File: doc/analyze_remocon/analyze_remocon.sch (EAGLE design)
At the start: 15 parts, among them IC3 PIC18F2550_28DIP, T1 2SC1815, X1 MINI-USB-UX60-MB-5S8

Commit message: update circuit diagram documents
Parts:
- removed C3, C4: (no value), rcl:C-EU025-024X044
- removed D1, D2: SFH482, led:SFH482
- removed JP1: (no value), pinhead:PINHD-1X5/90
- removed Q1: (no value), special:XTAL/S
- removed S1: PVA1R, switch-misc:PVA1R
- removed T1: 2SC1815, transistor:2SC1815
- added IRLED, IRLED1: (no value), led:LED3MM
- added Q2: BUZ11BV, transistor-power:BUZ11BV
- added R1, R2, R6, R7: (no value), rcl:R-US_MELF0102R
- added R10, R8, R9: (no value), rcl:R-US_0207/7
- added SW1, SW2: (no value), switch-omron:10-XX
- added Y1: (no value), xtal:CRES-HA
- C1, C2: device rcl:C-EU025-024X044 -> rcl:C-EUC0603K
- LED1, LED2: value LAP4-BOTTOM -> (none); device led:LAP4-BOTTOM -> led:LED3MM
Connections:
- removed net +5V: X1.1
- new net 20MHZ: IC3.OSC1/CLKI, Y1.LFT
- new net BLOCK: C1.1, IC3.VDD, R1.2, R10.2, R2.2, U$1.VCC, X1.1
- new net N$10: C2.1, IC3.VUSB
- new net N$11: LED1.A, R6.1
- new net N$12: IC3.RA5/AN4/!SS!/HLVDIN/C2OUT, R7.2
- new net N$13: LED2.A, R7.1
- new net N$14: IC3.RA0/AN0, R8.2, R9.1
- new net N$15: IRLED.A, R10.1
- new net N$16: IRLED.C, IRLED1.A
- new net N$17: IRLED1.C, Q2.D
- new net N$18: Q2.G, R9.2
- new net N$3: R1.1, SW1.P
- new net N$4: IC3.!MCLR!/VPP/RE3, SW1.P1
- new net N$5: R2.1, SW2.P
- new net N$6: IC3.RB4/AN11/KBI0/CSSPP, SW2.P1
- new net N$7: IC3.RB3/AN9/CCP2/VPO, U$1.VOUT
- new net N$8: IC3.RA6/OSC2/CLKO, Y1.RIT
- new net N$9: IC3.RA4/T0CKI/CIOUT/RCV, R6.2
- net GND: now also C1.2, C2.2, IC3.VSS, IC3.VSS@1, LED1.C, LED2.C, Q2.S, R8.1, SW1.S1, SW2.S1, U$1.GND, Y1.GND
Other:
- moved on the sheet: C1, C2, IC3, LED1, LED2, X1

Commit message: update circuit diagram documents
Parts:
- removed C1: (no value), rcl:C-EUC0603K
- added C3: (no value), rcl:C-EU025-025X050
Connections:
- removed net N$3: R1.1, SW1.P
- removed net N$5: R2.1, SW2.P
- removed net N$6: IC3.RB4/AN11/KBI0/CSSPP, SW2.P1
- new net N$7: IC3.RB4/AN11/KBI0/CSSPP, R2.1, SW2.P
- net BLOCK: now also C3.1; no longer C1.1
- net GND: now also C3.2, SW2.S; no longer C1.2
- net N$4: now also R1.1
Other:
- moved on the sheet: SW1, SW2
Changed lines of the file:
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@@
 <part name="LED2" library="led" deviceset="LED" device="3MM"/>
 <part name="Y1" library="xtal" deviceset="CRES-H" device="A"/>
-<part name="C1" library="rcl" deviceset="C-EU" device="C0603K"/>
 <part name="C2" library="rcl" deviceset="C-EU" device="C0603K"/>
 <part name="R1" library="rcl" deviceset="R-US_" device="MELF0102R"/>
@@
 <part name="R10" library="rcl" deviceset="R-US_" device="0207/7"/>
 <part name="Q2" library="transistor-power" deviceset="BUZ11" device="BV"/>
+<part name="C3" library="rcl" deviceset="C-EU" device="025-025X050"/>
+<part name="SUPPLY17" library="supply2" deviceset="GND" device=""/>
 </parts>
 <sheets>
@@
 <instance part="SUPPLY3" gate="+5V" x="96.52" y="17.78"/>
 <instance part="SUPPLY4" gate="GND" x="96.52" y="2.54"/>
-<instance part="SW1" gate="1" x="10.16" y="53.34" rot="R270"/>
-<instance part="SW2" gate="1" x="81.28" y="43.18" rot="R270"/>
+<instance part="SW1" gate="1" x="7.62" y="53.34" rot="R270"/>
+<instance part="SW2" gate="1" x="83.82" y="43.18" rot="R270"/>
 <instance part="SUPPLY5" gate="+5V" x="0" y="66.04"/>
-<instance part="SUPPLY6" gate="GND" x="15.24" y="48.26"/>
+<instance part="SUPPLY6" gate="GND" x="12.7" y="48.26"/>
 <instance part="SUPPLY7" gate="+5V" x="71.12" y="55.88"/>
 <instance part="SUPPLY8" gate="+5V" x="116.84" y="30.48"/>
 <instance part="SUPPLY9" gate="GND" x="104.14" y="27.94"/>
-<instance part="SUPPLY10" gate="GND" x="86.36" y="38.1"/>
+<instance part="SUPPLY10" gate="GND" x="88.9" y="38.1"/>
 <instance part="SUPPLY11" gate="GND" x="-12.7" y="-5.08"/>
 <instance part="SUPPLY12" gate="GND" x="-53.34" y="2.54"/>
@@
 <instance part="LED2" gate="G$1" x="-45.72" y="12.7" rot="R270"/>
 <instance part="Y1" gate="G$1" x="-30.48" y="-2.54"/>
-<instance part="C1" gate="G$1" x="96.52" y="12.7"/>
 <instance part="C2" gate="G$1" x="-5.08" y="2.54" rot="R270"/>
 <instance part="R1" gate="G$1" x="0" y="58.42" rot="R90"/>
@@
 <instance part="R10" gate="G$1" x="-15.24" y="71.12" rot="R90"/>
 <instance part="Q2" gate="1" x="-17.78" y="45.72"/>
+<instance part="C3" gate="G$1" x="96.52" y="12.7"/>
+<instance part="SUPPLY17" gate="GND" x="91.44" y="40.64"/>
 </instances>
 <busses>
@@
 <pinref part="SUPPLY3" gate="+5V" pin="+5V"/>
 <wire x1="73.66" y1="15.24" x2="96.52" y2="15.24" width="0.1524" layer="91"/>
-<pinref part="C1" gate="G$1" pin="1"/>
+<pinref part="C3" gate="G$1" pin="1"/>
 <junction x="96.52" y="15.24"/>
 </segment>
@@
 <pinref part="SUPPLY4" gate="GND" pin="GND"/>
 <wire x1="96.52" y1="7.62" x2="96.52" y2="5.08" width="0.1524" layer="91"/>
-<pinref part="C1" gate="G$1" pin="2"/>
+<pinref part="C3" gate="G$1" pin="2"/>
 <junction x="96.52" y="7.62"/>
 </segment>
@@
 <pinref part="SUPPLY15" gate="GND" pin="GND"/>
 </segment>
+<segment>
+<pinref part="SW2" gate="1" pin="S"/>
+<pinref part="SUPPLY17" gate="GND" pin="GND"/>
+<wire x1="88.9" y1="43.18" x2="91.44" y2="43.18" width="0.1524" layer="91"/>
+</segment>
 </net>
 <net name="N$1" class="0">
@@
 </segment>
 </net>
-<net name="N$5" class="0">
-<segment>
-<pinref part="SW2" gate="1" pin="P"/>
-<wire x1="71.12" y1="43.18" x2="76.2" y2="43.18" width="0.1524" layer="91"/>
-<pinref part="R2" gate="G$1" pin="1"/>
-</segment>
-</net>
-<net name="N$6" class="0">
-<segment>
-<pinref part="IC3" gate="G$1" pin="RB4/AN11/KBI0/CSSPP"/>
-<pinref part="SW2" gate="1" pin="P1"/>
-<wire x1="73.66" y1="27.94" x2="76.2" y2="27.94" width="0.1524" layer="91"/>
-<wire x1="76.2" y1="27.94" x2="76.2" y2="40.64" width="0.1524" layer="91"/>
-</segment>
-</net>
-<net name="N$7" class="0">
+<net name="N$19" class="0">
 <segment>
 <pinref part="IC3" gate="G$1" pin="RB3/AN9/CCP2/VPO"/>
@@
 <pinref part="SW1" gate="1" pin="P1"/>
 <pinref part="IC3" gate="G$1" pin="!MCLR!/VPP/RE3"/>
-<wire x1="5.08" y1="50.8" x2="-2.54" y2="50.8" width="0.1524" layer="91"/>
+<wire x1="2.54" y1="50.8" x2="0" y2="50.8" width="0.1524" layer="91"/>
+<wire x1="0" y1="50.8" x2="-2.54" y2="50.8" width="0.1524" layer="91"/>
 <wire x1="-2.54" y1="50.8" x2="-2.54" y2="35.56" width="0.1524" layer="91"/>
-</segment>
-</net>
-<net name="N$3" class="0">
-<segment>
-<pinref part="SW1" gate="1" pin="P"/>
-<wire x1="0" y1="53.34" x2="5.08" y2="53.34" width="0.1524" layer="91"/>
 <pinref part="R1" gate="G$1" pin="1"/>
+<wire x1="0" y1="50.8" x2="0" y2="53.34" width="0.1524" layer="91"/>
+<junction x="0" y="50.8"/>
 </segment>
 </net>
@@
 </segment>
 </net>
+<net name="N$7" class="0">
+<segment>
+<pinref part="SW2" gate="1" pin="P"/>
+<wire x1="71.12" y1="43.18" x2="76.2" y2="43.18" width="0.1524" layer="91"/>
+<pinref part="R2" gate="G$1" pin="1"/>
+<pinref part="IC3" gate="G$1" pin="RB4/AN11/KBI0/CSSPP"/>
+<wire x1="76.2" y1="43.18" x2="78.74" y2="43.18" width="0.1524" layer="91"/>
+<wire x1="73.66" y1="27.94" x2="76.2" y2="27.94" width="0.1524" layer="91"/>
+<wire x1="76.2" y1="27.94" x2="76.2" y2="43.18" width="0.1524" layer="91"/>
+<junction x="76.2" y="43.18"/>
+</segment>
+</net>

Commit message: update circuit diagram documents
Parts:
- removed C3: (no value), rcl:C-EU025-025X050
- removed R8, R9: (no value), rcl:R-US_0207/7
- added C1: 0.1uF, rcl:C-EU025-024X044
- added R3, R4: 1KΩ, rcl:R-US_MELF0102R
- C2: value (none) -> 0.1uF; device rcl:C-EUC0603K -> rcl:C-EU025-024X044
- IRLED1, IRLED2: value (none) -> TLN105B
- R1, R2: value (none) -> 10KΩ
- R5: value (none) -> 1Ω
- R6, R7: value (none) -> 10KΩ; device rcl:R-US_MELF0102R -> rcl:R-US_0207/7
- RESONATOR: value (none) -> 20MHz
- renumbered IRLED to IRLED2, Q2 to 2SK2201, R10 to R5, U$1 to PL-IRM2161-C438, Y1 to RESONATOR
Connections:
- net BLOCK: now also C1.1; no longer C3.1
- net GND: now also C1.2, R6.1; no longer C3.2, R8.1
- net N$11: now also R3.1; no longer R6.1
- net N$12: now also R4.2; no longer R7.2
- net N$13: now also R4.1; no longer R7.1
- net N$14: now also R6.2, R7.1; no longer R8.2, R9.1
- net N$18: now also R7.2; no longer R9.2
- net N$9: now also R3.2; no longer R6.2
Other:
- moved on the sheet: R6, R7
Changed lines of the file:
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@@
 <part name="IC3" library="microchip" deviceset="PIC18F2*_28" device="DIP" technology="550"/>
 <part name="X1" library="con-hirose" deviceset="MINI-USB-" device="UX60-MB-5S8"/>
-<part name="U$1" library="IRM2161" deviceset="IRM2161" device=""/>
+<part name="PL-IRM2161-C438" library="IRM2161" deviceset="IRM2161" device=""/>
 <part name="SUPPLY1" library="supply2" deviceset="GND" device=""/>
 <part name="SUPPLY2" library="supply2" deviceset="+5V" device=""/>
@@
 <part name="LED1" library="led" deviceset="LED" device="3MM"/>
 <part name="LED2" library="led" deviceset="LED" device="3MM"/>
-<part name="Y1" library="xtal" deviceset="CRES-H" device="A"/>
-<part name="C2" library="rcl" deviceset="C-EU" device="C0603K"/>
-<part name="R1" library="rcl" deviceset="R-US_" device="MELF0102R"/>
-<part name="R2" library="rcl" deviceset="R-US_" device="MELF0102R"/>
-<part name="R6" library="rcl" deviceset="R-US_" device="MELF0102R"/>
-<part name="R7" library="rcl" deviceset="R-US_" device="MELF0102R"/>
-<part name="IRLED" library="led" deviceset="LED" device="3MM"/>
-<part name="IRLED1" library="led" deviceset="LED" device="3MM"/>
-<part name="R8" library="rcl" deviceset="R-US_" device="0207/7"/>
-<part name="R9" library="rcl" deviceset="R-US_" device="0207/7"/>
-<part name="R10" library="rcl" deviceset="R-US_" device="0207/7"/>
-<part name="Q2" library="transistor-power" deviceset="BUZ11" device="BV"/>
-<part name="C3" library="rcl" deviceset="C-EU" device="025-025X050"/>
+<part name="RESONATOR" library="xtal" deviceset="CRES-H" device="A" value="20MHz"/>
+<part name="R1" library="rcl" deviceset="R-US_" device="MELF0102R" value="10KΩ"/>
+<part name="R2" library="rcl" deviceset="R-US_" device="MELF0102R" value="10KΩ"/>
+<part name="R3" library="rcl" deviceset="R-US_" device="MELF0102R" value="1KΩ"/>
+<part name="R4" library="rcl" deviceset="R-US_" device="MELF0102R" value="1KΩ"/>
+<part name="IRLED2" library="led" deviceset="LED" device="3MM" value="TLN105B"/>
+<part name="IRLED1" library="led" deviceset="LED" device="3MM" value="TLN105B"/>
+<part name="R6" library="rcl" deviceset="R-US_" device="0207/7" value="10KΩ"/>
+<part name="R7" library="rcl" deviceset="R-US_" device="0207/7" value="10KΩ"/>
+<part name="R5" library="rcl" deviceset="R-US_" device="0207/7" value="1Ω"/>
+<part name="2SK2201" library="transistor-power" deviceset="BUZ11" device="BV" value=""/>
 <part name="SUPPLY17" library="supply2" deviceset="GND" device=""/>
+<part name="C1" library="rcl" deviceset="C-EU" device="025-024X044" value="0.1uF"/>
+<part name="C2" library="rcl" deviceset="C-EU" device="025-024X044" value="0.1uF"/>
 </parts>
 <sheets>
@@
 <instance part="IC3" gate="G$1" x="35.56" y="20.32"/>
 <instance part="X1" gate="G$1" x="78.74" y="-12.7" rot="R270"/>
-<instance part="U$1" gate="G$1" x="104.14" y="48.26"/>
+<instance part="PL-IRM2161-C438" gate="G$1" x="104.14" y="48.26"/>
 <instance part="SUPPLY1" gate="GND" x="63.5" y="-12.7"/>
 <instance part="SUPPLY2" gate="+5V" x="83.82" y="-2.54"/>
@@
 <instance part="LED1" gate="G$1" x="-45.72" y="22.86" rot="R270"/>
 <instance part="LED2" gate="G$1" x="-45.72" y="12.7" rot="R270"/>
-<instance part="Y1" gate="G$1" x="-30.48" y="-2.54"/>
-<instance part="C2" gate="G$1" x="-5.08" y="2.54" rot="R270"/>
+<instance part="RESONATOR" gate="G$1" x="-30.48" y="-2.54"/>
 <instance part="R1" gate="G$1" x="0" y="58.42" rot="R90"/>
 <instance part="R2" gate="G$1" x="71.12" y="48.26" rot="R90"/>
-<instance part="R6" gate="G$1" x="-38.1" y="22.86"/>
-<instance part="R7" gate="G$1" x="-38.1" y="12.7"/>
-<instance part="IRLED" gate="G$1" x="-15.24" y="63.5"/>
+<instance part="R3" gate="G$1" x="-38.1" y="22.86"/>
+<instance part="R4" gate="G$1" x="-38.1" y="12.7"/>
+<instance part="IRLED2" gate="G$1" x="-15.24" y="63.5"/>
 <instance part="IRLED1" gate="G$1" x="-15.24" y="55.88"/>
-<instance part="R8" gate="G$1" x="-30.48" y="38.1" rot="R90"/>
-<instance part="R9" gate="G$1" x="-25.4" y="43.18"/>
-<instance part="R10" gate="G$1" x="-15.24" y="71.12" rot="R90"/>
-<instance part="Q2" gate="1" x="-17.78" y="45.72"/>
-<instance part="C3" gate="G$1" x="96.52" y="12.7"/>
+<instance part="R6" gate="G$1" x="-30.48" y="38.1" rot="R90"/>
+<instance part="R7" gate="G$1" x="-25.4" y="43.18"/>
+<instance part="R5" gate="G$1" x="-15.24" y="71.12" rot="R90"/>
+<instance part="2SK2201" gate="1" x="-17.78" y="45.72"/>
 <instance part="SUPPLY17" gate="GND" x="91.44" y="40.64"/>
+<instance part="C1" gate="G$1" x="96.52" y="12.7"/>
+<instance part="C2" gate="G$1" x="-5.08" y="2.54" rot="R270"/>
 </instances>
 <busses>
@@
 <pinref part="SUPPLY3" gate="+5V" pin="+5V"/>
 <wire x1="73.66" y1="15.24" x2="96.52" y2="15.24" width="0.1524" layer="91"/>
-<pinref part="C3" gate="G$1" pin="1"/>
+<pinref part="C1" gate="G$1" pin="1"/>
 <junction x="96.52" y="15.24"/>
 </segment>
 <segment>
-<pinref part="U$1" gate="G$1" pin="VCC"/>
+<pinref part="PL-IRM2161-C438" gate="G$1" pin="VCC"/>
 <wire x1="109.22" y1="30.48" x2="109.22" y2="27.94" width="0.1524" layer="91"/>
 <pinref part="SUPPLY8" gate="+5V" pin="+5V"/>
@@
 <segment>
 <pinref part="SUPPLY14" gate="+5V" pin="+5V"/>
-<pinref part="R10" gate="G$1" pin="2"/>
+<pinref part="R5" gate="G$1" pin="2"/>
 </segment>
 </net>
@@
 <pinref part="SUPPLY4" gate="GND" pin="GND"/>
 <wire x1="96.52" y1="7.62" x2="96.52" y2="5.08" width="0.1524" layer="91"/>
-<pinref part="C3" gate="G$1" pin="2"/>
+<pinref part="C1" gate="G$1" pin="2"/>
 <junction x="96.52" y="7.62"/>
 </segment>
 <segment>
-<pinref part="U$1" gate="G$1" pin="GND"/>
+<pinref part="PL-IRM2161-C438" gate="G$1" pin="GND"/>
 <pinref part="SUPPLY9" gate="GND" pin="GND"/>
 </segment>
@@
 <segment>
 <pinref part="SUPPLY13" gate="GND" pin="GND"/>
-<pinref part="Y1" gate="G$1" pin="GND"/>
+<pinref part="RESONATOR" gate="G$1" pin="GND"/>
 </segment>
 <segment>
 <pinref part="SUPPLY16" gate="GND" pin="GND"/>
-<pinref part="R8" gate="G$1" pin="1"/>
-</segment>
-<segment>
-<pinref part="Q2" gate="1" pin="S"/>
+<pinref part="R6" gate="G$1" pin="1"/>
+</segment>
+<segment>
+<pinref part="2SK2201" gate="1" pin="S"/>
 <pinref part="SUPPLY15" gate="GND" pin="GND"/>
 </segment>
@@
 <segment>
 <pinref part="IC3" gate="G$1" pin="RB3/AN9/CCP2/VPO"/>
-<pinref part="U$1" gate="G$1" pin="VOUT"/>
+<pinref part="PL-IRM2161-C438" gate="G$1" pin="VOUT"/>
 <wire x1="73.66" y1="25.4" x2="99.06" y2="25.4" width="0.1524" layer="91"/>
 <wire x1="99.06" y1="25.4" x2="99.06" y2="30.48" width="0.1524" layer="91"/>
@@
 <wire x1="-20.32" y1="-2.54" x2="-20.32" y2="12.7" width="0.1524" layer="91"/>
 <wire x1="-20.32" y1="12.7" x2="-2.54" y2="12.7" width="0.1524" layer="91"/>
-<pinref part="Y1" gate="G$1" pin="RIT"/>
+<pinref part="RESONATOR" gate="G$1" pin="RIT"/>
 </segment>
 </net>
@@
 <wire x1="-22.86" y1="5.08" x2="-38.1" y2="5.08" width="0.1524" layer="91"/>
 <wire x1="-38.1" y1="5.08" x2="-38.1" y2="-2.54" width="0.1524" layer="91"/>
-<pinref part="Y1" gate="G$1" pin="LFT"/>
+<pinref part="RESONATOR" gate="G$1" pin="LFT"/>
 </segment>
 </net>
@@
 <pinref part="IC3" gate="G$1" pin="RA4/T0CKI/CIOUT/RCV"/>
 <wire x1="-2.54" y1="22.86" x2="-33.02" y2="22.86" width="0.1524" layer="91"/>
-<pinref part="R6" gate="G$1" pin="2"/>
+<pinref part="R3" gate="G$1" pin="2"/>
 </segment>
 </net>
@@
 <pinref part="IC3" gate="G$1" pin="RA5/AN4/!SS!/HLVDIN/C2OUT"/>
 <wire x1="-33.02" y1="20.32" x2="-2.54" y2="20.32" width="0.1524" layer="91"/>
-<pinref part="R7" gate="G$1" pin="2"/>
-</segment>
-</net>
-<net name="N$10" class="0">
-<segment>
-<pinref part="IC3" gate="G$1" pin="VUSB"/>
-<pinref part="C2" gate="G$1" pin="1"/>
+<pinref part="R4" gate="G$1" pin="2"/>
 </segment>
 </net>
@@
 <segment>
 <pinref part="LED1" gate="G$1" pin="A"/>
-<pinref part="R6" gate="G$1" pin="1"/>
+<pinref part="R3" gate="G$1" pin="1"/>
 </segment>
 </net>
@@
 <segment>
 <pinref part="LED2" gate="G$1" pin="A"/>
-<pinref part="R7" gate="G$1" pin="1"/>
+<pinref part="R4" gate="G$1" pin="1"/>
 </segment>
 </net>
@@
 <wire x1="-7.62" y1="86.36" x2="-30.48" y2="86.36" width="0.1524" layer="91"/>
 <wire x1="-30.48" y1="86.36" x2="-30.48" y2="43.18" width="0.1524" layer="91"/>
-<pinref part="R9" gate="G$1" pin="1"/>
-<pinref part="R8" gate="G$1" pin="2"/>
+<pinref part="R7" gate="G$1" pin="1"/>
+<pinref part="R6" gate="G$1" pin="2"/>
 <junction x="-30.48" y="43.18"/>
 </segment>
@@
 <net name="N$16" class="0">
 <segment>
-<pinref part="IRLED" gate="G$1" pin="C"/>
+<pinref part="IRLED2" gate="G$1" pin="C"/>
 <pinref part="IRLED1" gate="G$1" pin="A"/>
 </segment>
@@
 <net name="N$15" class="0">
 <segment>
-<pinref part="IRLED" gate="G$1" pin="A"/>
-<pinref part="R10" gate="G$1" pin="1"/>
+<pinref part="IRLED2" gate="G$1" pin="A"/>
+<pinref part="R5" gate="G$1" pin="1"/>
 </segment>
 </net>
@@
 <segment>
 <pinref part="IRLED1" gate="G$1" pin="C"/>
-<pinref part="Q2" gate="1" pin="D"/>
+<pinref part="2SK2201" gate="1" pin="D"/>
 </segment>
 </net>
 <net name="N$18" class="0">
 <segment>
-<pinref part="Q2" gate="1" pin="G"/>
-<pinref part="R9" gate="G$1" pin="2"/>
+<pinref part="2SK2201" gate="1" pin="G"/>
+<pinref part="R7" gate="G$1" pin="2"/>
 </segment>
 </net>
@@
 </segment>
 </net>
+<net name="N$3" class="0">
+<segment>
+<pinref part="IC3" gate="G$1" pin="VUSB"/>
+<pinref part="C2" gate="G$1" pin="1"/>
+</segment>
+</net>

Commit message: update circuit diagram documents
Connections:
- net GND: no longer SW2.S
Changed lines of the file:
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@@
 <part name="R5" library="rcl" deviceset="R-US_" device="0207/7" value="1Ω"/>
 <part name="2SK2201" library="transistor-power" deviceset="BUZ11" device="BV" value=""/>
-<part name="SUPPLY17" library="supply2" deviceset="GND" device=""/>
 <part name="C1" library="rcl" deviceset="C-EU" device="025-024X044" value="0.1uF"/>
 <part name="C2" library="rcl" deviceset="C-EU" device="025-024X044" value="0.1uF"/>
@@
 <instance part="R5" gate="G$1" x="-15.24" y="71.12" rot="R90"/>
 <instance part="2SK2201" gate="1" x="-17.78" y="45.72"/>
-<instance part="SUPPLY17" gate="GND" x="91.44" y="40.64"/>
 <instance part="C1" gate="G$1" x="96.52" y="12.7"/>
 <instance part="C2" gate="G$1" x="-5.08" y="2.54" rot="R270"/>
@@
 <pinref part="SUPPLY15" gate="GND" pin="GND"/>
 </segment>
-<segment>
-<pinref part="SW2" gate="1" pin="S"/>
-<pinref part="SUPPLY17" gate="GND" pin="GND"/>
-<wire x1="88.9" y1="43.18" x2="91.44" y2="43.18" width="0.1524" layer="91"/>
-</segment>
 </net>

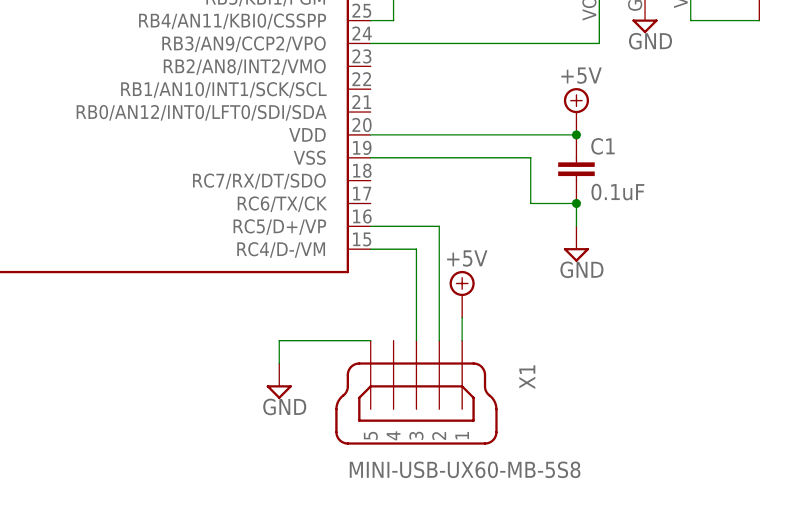
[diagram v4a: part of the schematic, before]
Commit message: update circuit diagram documents. fix D+ D- line.
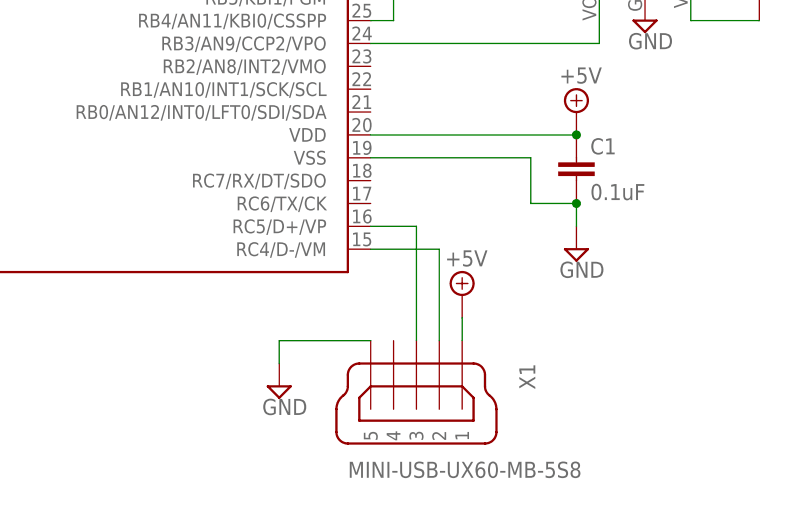
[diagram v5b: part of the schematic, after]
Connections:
- net N$1: now also IC3.RC4/D-/VM; no longer IC3.RC5/D+/VP
- net N$2: now also IC3.RC5/D+/VP; no longer IC3.RC4/D-/VM
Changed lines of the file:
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@@
 <net name="N$1" class="0">
 <segment>
-<pinref part="IC3" gate="G$1" pin="RC5/D+/VP"/>
 <pinref part="X1" gate="G$1" pin="2"/>
-<wire x1="73.66" y1="5.08" x2="81.28" y2="5.08" width="0.1524" layer="91"/>
-<wire x1="81.28" y1="5.08" x2="81.28" y2="-7.62" width="0.1524" layer="91"/>
-</segment>
-</net>
-<net name="N$2" class="0">
-<segment>
+<wire x1="81.28" y1="2.54" x2="81.28" y2="-7.62" width="0.1524" layer="91"/>
 <pinref part="IC3" gate="G$1" pin="RC4/D-/VM"/>
-<pinref part="X1" gate="G$1" pin="3"/>
-<wire x1="73.66" y1="2.54" x2="78.74" y2="2.54" width="0.1524" layer="91"/>
-<wire x1="78.74" y1="2.54" x2="78.74" y2="-7.62" width="0.1524" layer="91"/>
+<wire x1="73.66" y1="2.54" x2="81.28" y2="2.54" width="0.1524" layer="91"/>
 </segment>
 </net>
@@
 </segment>
 </net>
+<net name="N$2" class="0">
+<segment>
+<pinref part="IC3" gate="G$1" pin="RC5/D+/VP"/>
+<pinref part="X1" gate="G$1" pin="3"/>
+<wire x1="73.66" y1="5.08" x2="78.74" y2="5.08" width="0.1524" layer="91"/>
+<wire x1="78.74" y1="5.08" x2="78.74" y2="-7.62" width="0.1524" layer="91"/>
+</segment>
+</net>
